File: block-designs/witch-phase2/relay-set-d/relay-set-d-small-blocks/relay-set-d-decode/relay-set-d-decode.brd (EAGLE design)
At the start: 98.8 x 75.2 mm, 67 parts, among them IC1 74LS138D, IC13 74LVC1G125DBV, IC14 74LVC1G125DBV, IC15 74LVC1G125DBV, IC16 74LVC1G125DBV, IC17 74LVC1G125DBV, IC18 74LVC1G125DBV, IC19 74LVC1G125DBV, IC2 74LS138D, IC20 74LVC1G125DBV, IC21 74LVC1G125DBV, IC22 74LVC1G125DBV, IC3 74LS138D, IC4 74LS138D

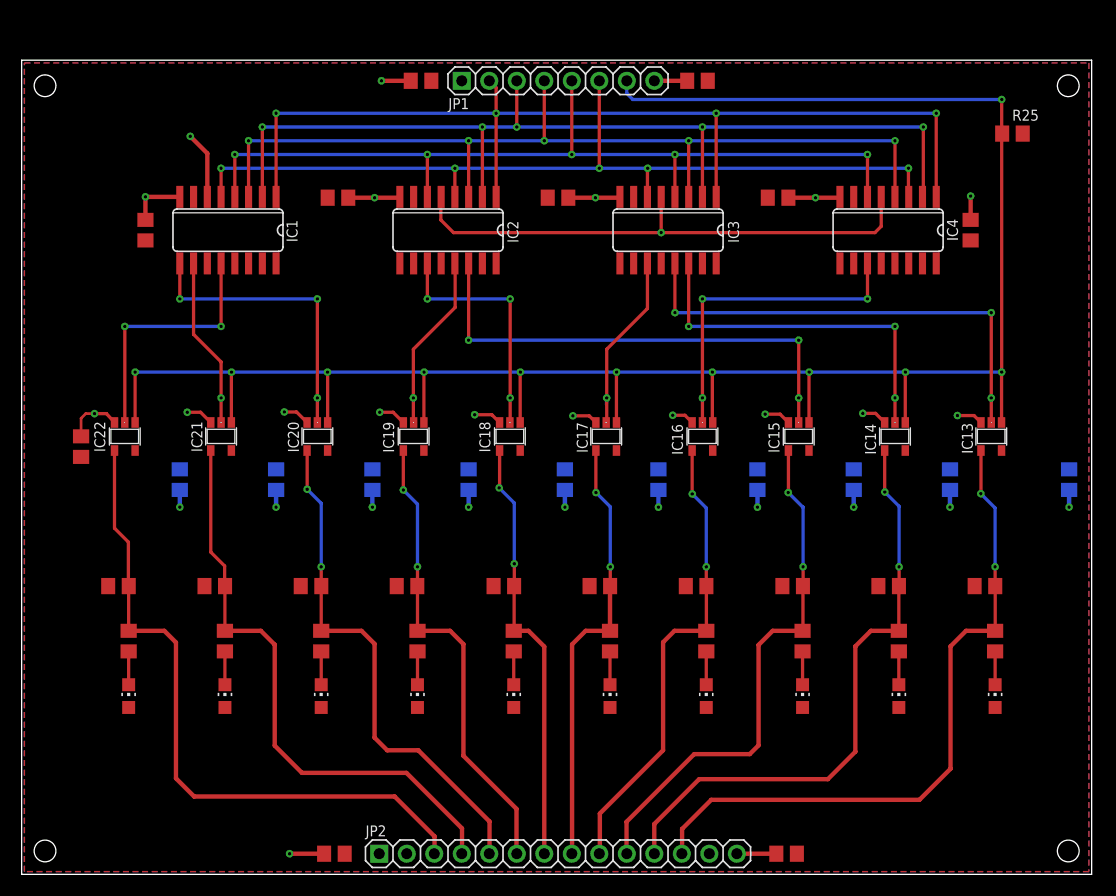
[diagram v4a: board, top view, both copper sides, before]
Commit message: updated layout for easy interface to the rest of the system
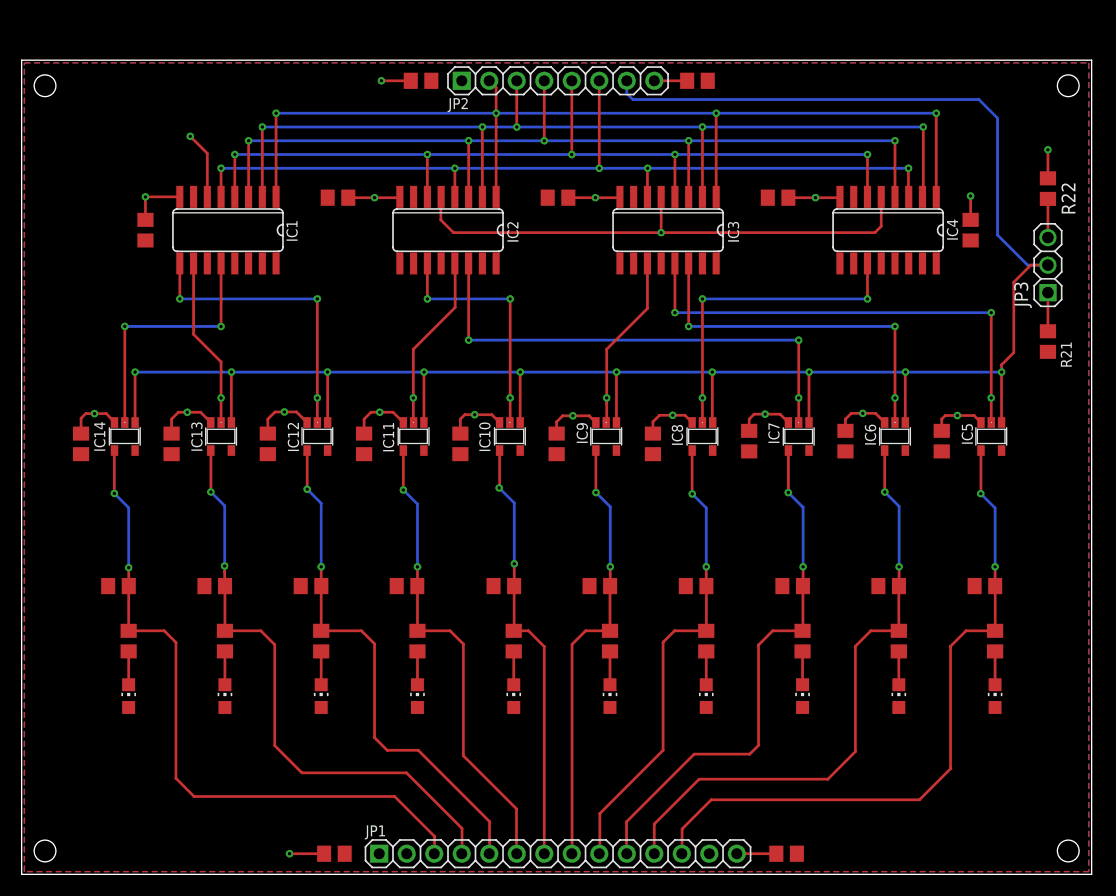
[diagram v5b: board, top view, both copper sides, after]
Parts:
- removed C20: (no value), resistor:C0805
- removed IC21, IC22: 74LVC1G125DBV, 74xx-little-us:SOT23-5
- removed R25: (no value), resistor:R0805
- added IC5, IC6: 74LVC1G125DBV, 74xx-little-us:SOT23-5
- added JP3: (no value), pinhead:1X03
- added R21, R22: (no value), resistor:R0805
- JP1: device pinhead:1X08 -> pinhead:1X14
- JP2: device pinhead:1X14 -> pinhead:1X08
- moved JP1 71.4 mm to (49.5, 1.91)
- moved JP2 71.4 mm to (49.5, 73.3)
- moved IC13 71.1 mm to (18.4, 40.4)
- moved IC14 71.1 mm to (9.53, 40.4)
- moved C16 65.2 mm to (31.6, 39.8), flipped to the top
- moved C18 8.77 mm to (40.5, 39.8), flipped to the top
- moved C12 3.64 mm to (76.1, 40.0), flipped to the top
- moved C14 3.64 mm to (85.0, 40.0), flipped to the top
- moved C10 3.64 mm to (67.2, 40.0), flipped to the top
- moved C15 3.39 mm to (13.8, 39.8), flipped to the top
- moved C17 3.39 mm to (22.7, 39.8), flipped to the top
- moved C6 3.39 mm to (49.4, 39.8), flipped to the top
- moved C8 3.34 mm to (58.3, 39.8), flipped to the top
- moved C13 0.25 mm to (5.49, 39.8)
- renumbered IC15 to IC7, IC16 to IC8, IC17 to IC9, IC18 to IC10, IC19 to IC11, IC20 to IC12
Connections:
- removed net !ONE-NINE_OUT: JP2.13
- removed net !ZERO_OUT: JP2.2
- new net N$11: JP3.1, R21.1
- new net N$13: JP3.3, R22.2
- net DA_IN: now also JP2.2; no longer JP1.2
- net DB_IN: now also JP2.3; no longer JP1.3
- net DC_IN: now also JP2.4; no longer JP1.4
- net DD_IN: now also JP2.5; no longer JP1.5
- net DE_IN: now also JP2.6; no longer JP1.6
- net DSA-DSB: now also IC5.1, IC6.1, JP2.7, JP3.2; no longer IC21.1, IC22.1, JP1.7, R25.1
- net EIGHT: now also IC6.2; no longer IC14.2
- net EIGHT_N: now also IC6.4, JP1.11; no longer IC14.4, JP2.11
- net FIVE_N: now also JP1.8; no longer JP2.8
- net FOUR_N: now also JP1.7; no longer JP2.7
- net GND: now also IC5.3, IC6.3, JP1.14, JP2.8, R22.1; no longer C20.2, IC21.3, IC22.3, JP1.8, JP2.14
- net NINE: now also IC5.2; no longer IC13.2
- net NINE_N: now also IC5.4, JP1.12; no longer IC13.4, JP2.12
- net ONE: now also IC13.2; no longer IC21.2
- net ONE_N: now also IC13.4, JP1.4; no longer IC21.4, JP2.4
- net SEVEN_N: now also JP1.10; no longer JP2.10
- net SIX_N: now also JP1.9; no longer JP2.9
- net THREE_N: now also JP1.6; no longer JP2.6
- net TWO_N: now also JP1.5; no longer JP2.5
- net VCC: now also IC5.5, IC6.5, R21.2; no longer C20.1, IC21.5, IC22.5, R25.2
- net ZERO: now also IC14.2; no longer IC22.2
- net ZERO_N: now also IC14.4, JP1.3; no longer IC22.4, JP2.3
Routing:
- net GND: track 111.6 -> 140.3 mm, vias 18 -> 19
- net VCC: track 22.1 -> 6.24 mm, vias 11 -> 1
- net DSA-DSB: track 187.9 -> 192.2 mm, vias 11 -> 10
- net N$13: track 0.00 -> 3.57 mm
- net N$11: track 0.00 -> 3.57 mm
- net ZERO_N: vias 0 -> 2
- net ONE_N: vias 0 -> 2
